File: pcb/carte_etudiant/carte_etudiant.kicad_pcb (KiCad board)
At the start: 2 copper layers, 76 x 83 mm, 5 parts, among them J1 Conn_02x15_Odd_Even, J2 Conn_01x14, J3 Conn_01x14, U1 NUCLEO64-F103RB

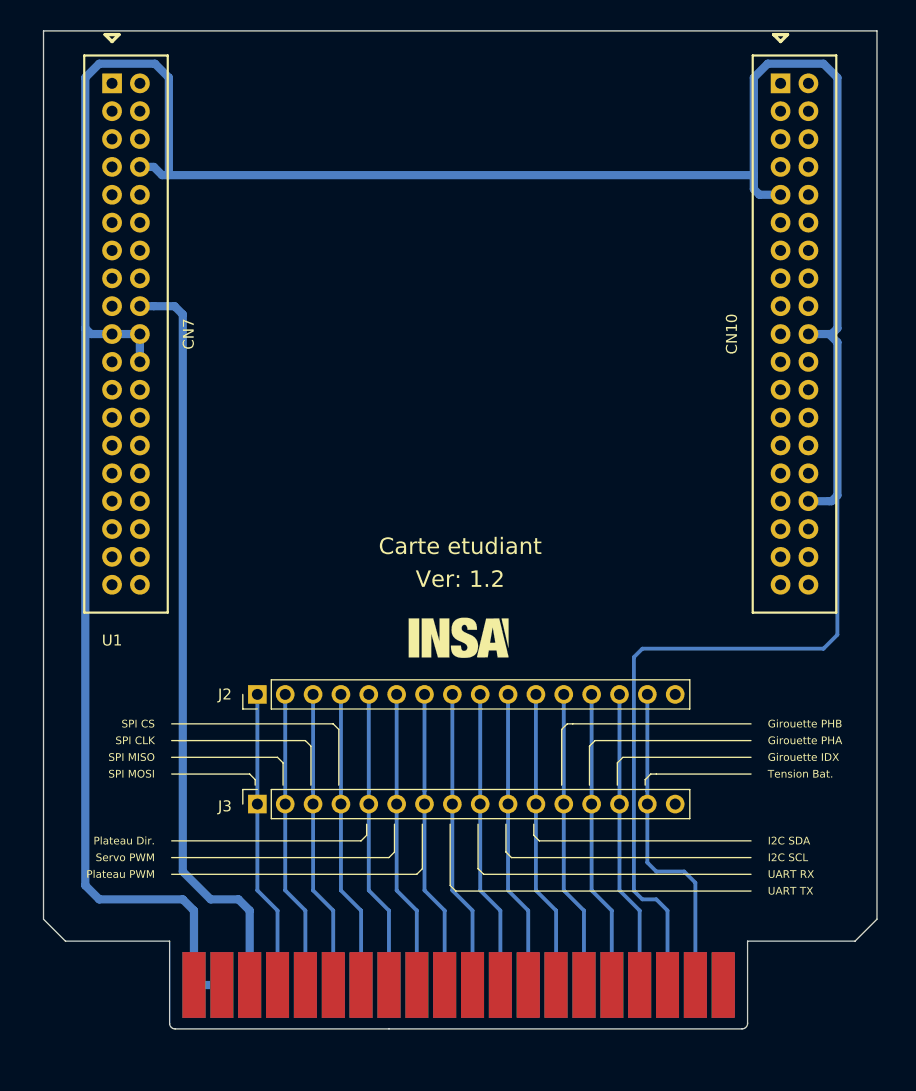
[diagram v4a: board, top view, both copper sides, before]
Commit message: Modification de la taille de la serigraphie et de son oreintation pour les cartes etudiant
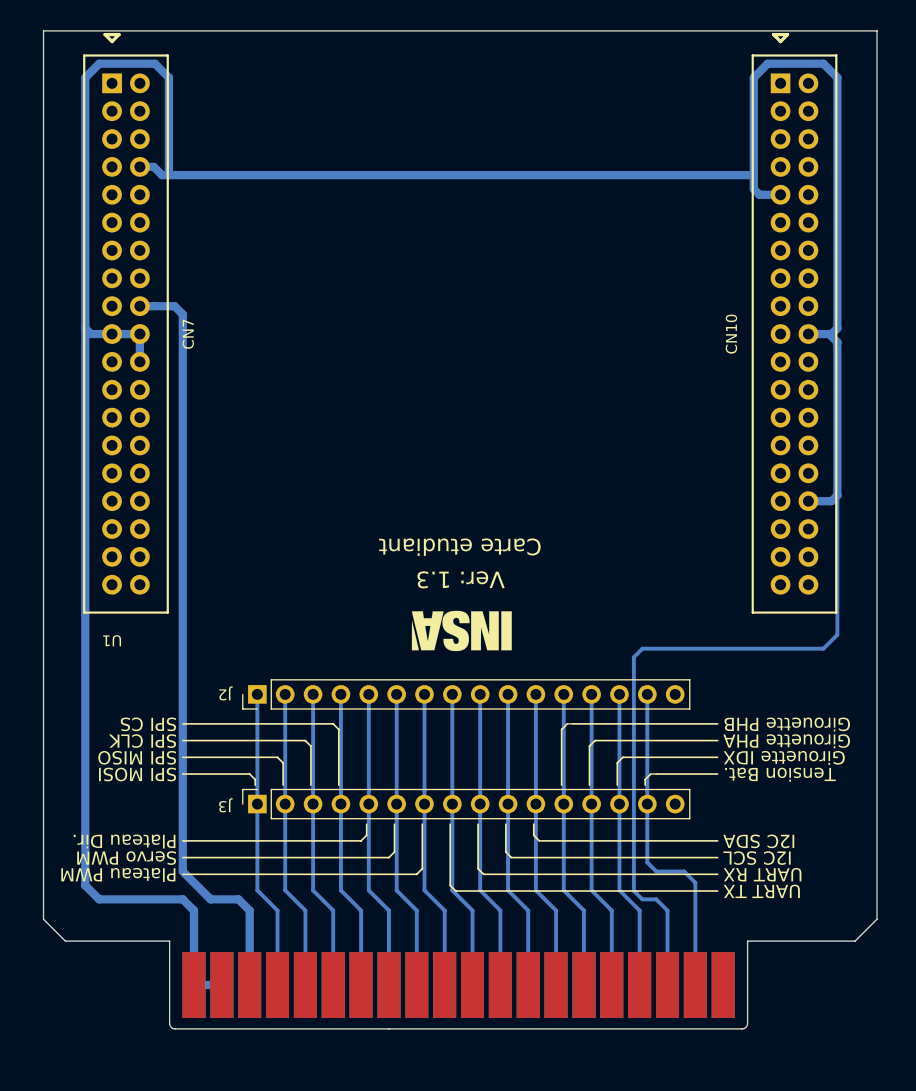
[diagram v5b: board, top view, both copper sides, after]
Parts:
- moved G*** 0.95 mm to (127.0, 117.6), turned to 180 degrees
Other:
- board text added: "Ver: 1.3"
- board text removed: "Ver: 1.2"

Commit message: rajout de plot de masse + changement taille serigraphie sur carte-etudiant
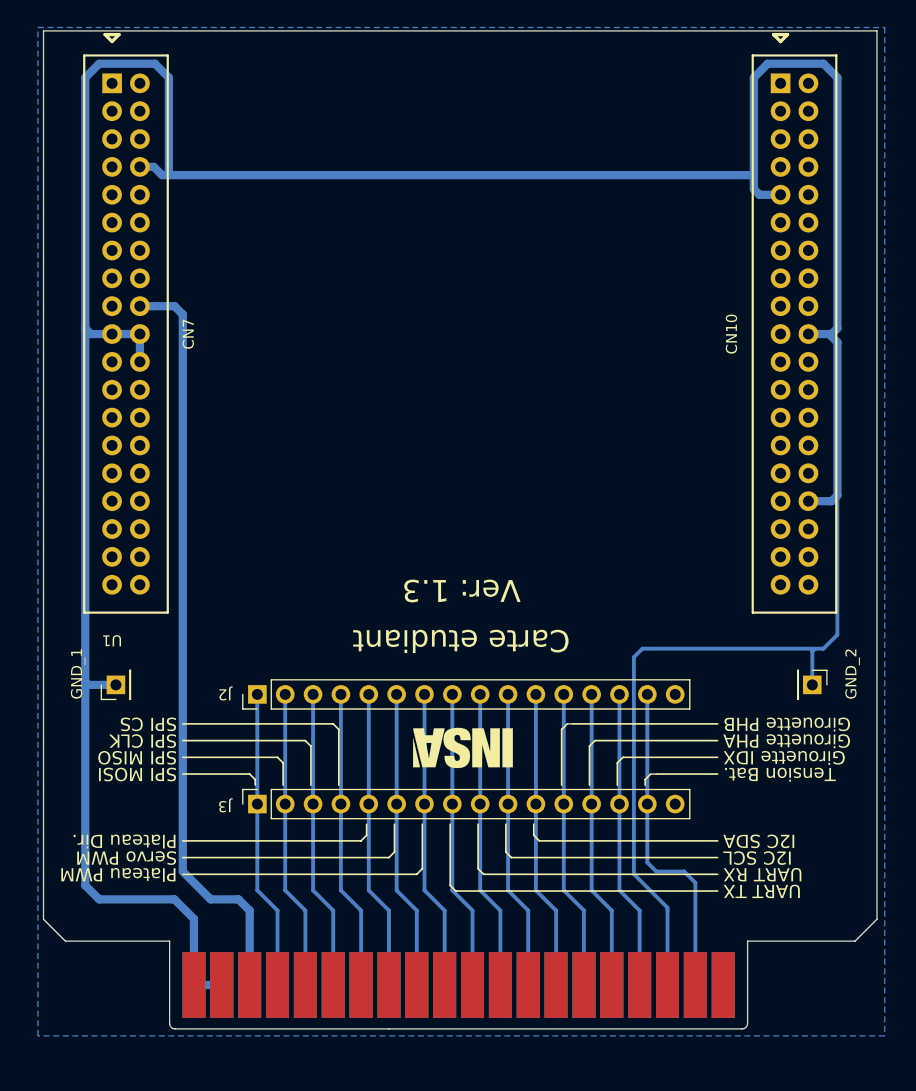
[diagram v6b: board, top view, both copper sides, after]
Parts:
- removed G***: LOGO, Insa:insa-image
- added G1: LOGO, Insa:insa-image, F.Cu at (127.1, 128.2)
- added GND_1: GND Ref, Connector_PinHeader_2.54mm:PinHeader_1x01_P2.54mm_Vertical, F.Cu at (95.6, 122.6)
- added GND_2: GND Ref, Connector_PinHeader_2.54mm:PinHeader_1x01_P2.54mm_Vertical, F.Cu at (159.1, 122.6)
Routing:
- net GND: track 304.5 -> 309.7 mm
- added copper zone on B.Cu, net GND

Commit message: Version 1.4 de la carte etudiant, ajout de la ligne SPI_CS2
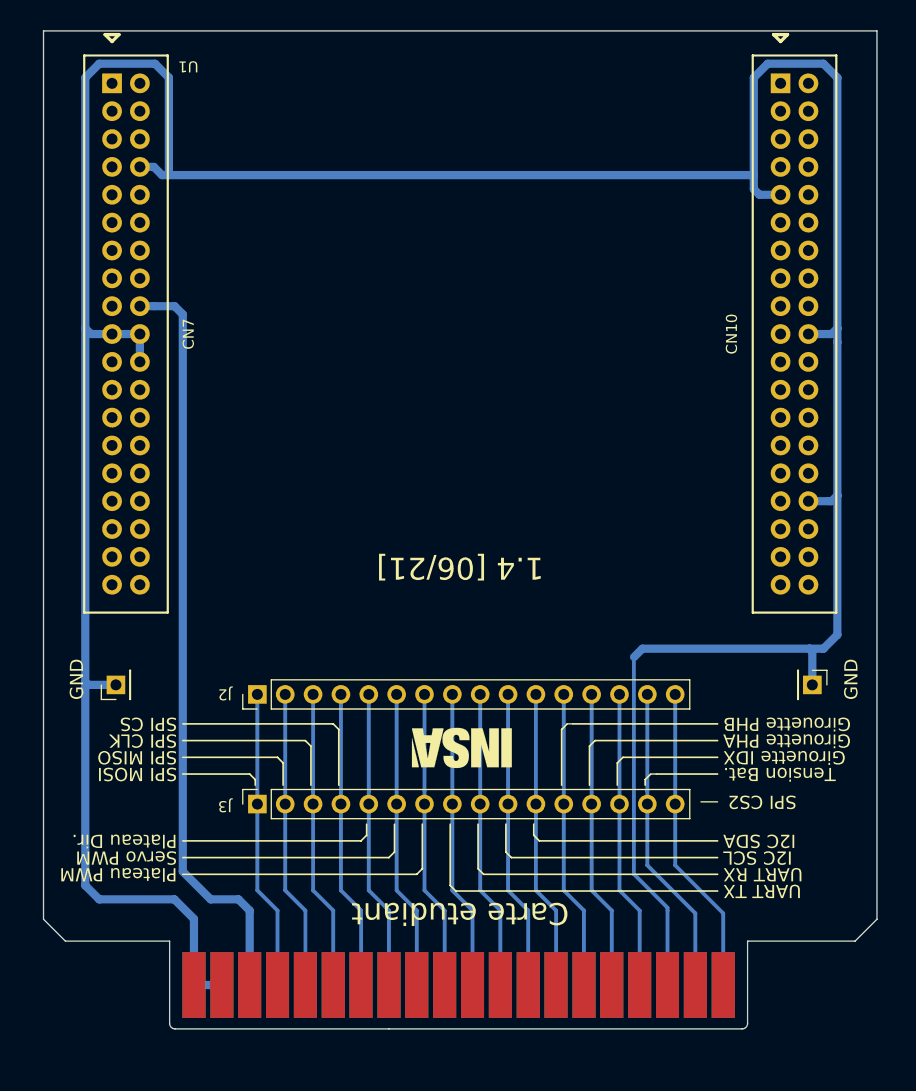
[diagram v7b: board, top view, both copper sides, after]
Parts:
- removed G1: LOGO, Insa:insa-image
- added G***: LOGO, Insa:insa-image, F.Cu at (127.0, 128.2)
- renumbered GND_2 to GND, GND_1 to GND
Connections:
- J1 pad 40: (no net) -> /SPI_CS2
- J2 pad 16: (no net) -> /SPI_CS2
- J3 pad 16: (no net) -> /SPI_CS2
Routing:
- net /SPI_CS2: track 0.00 -> 28.3 mm
- net /TENSION_BATTERIE: track 29.8 -> 28.3 mm
- removed copper zone on B.Cu, net GND
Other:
- board text added: "1.4 [06/21]"
- board text added: "SPI CS2"
- board text removed: "Ver: 1.3"

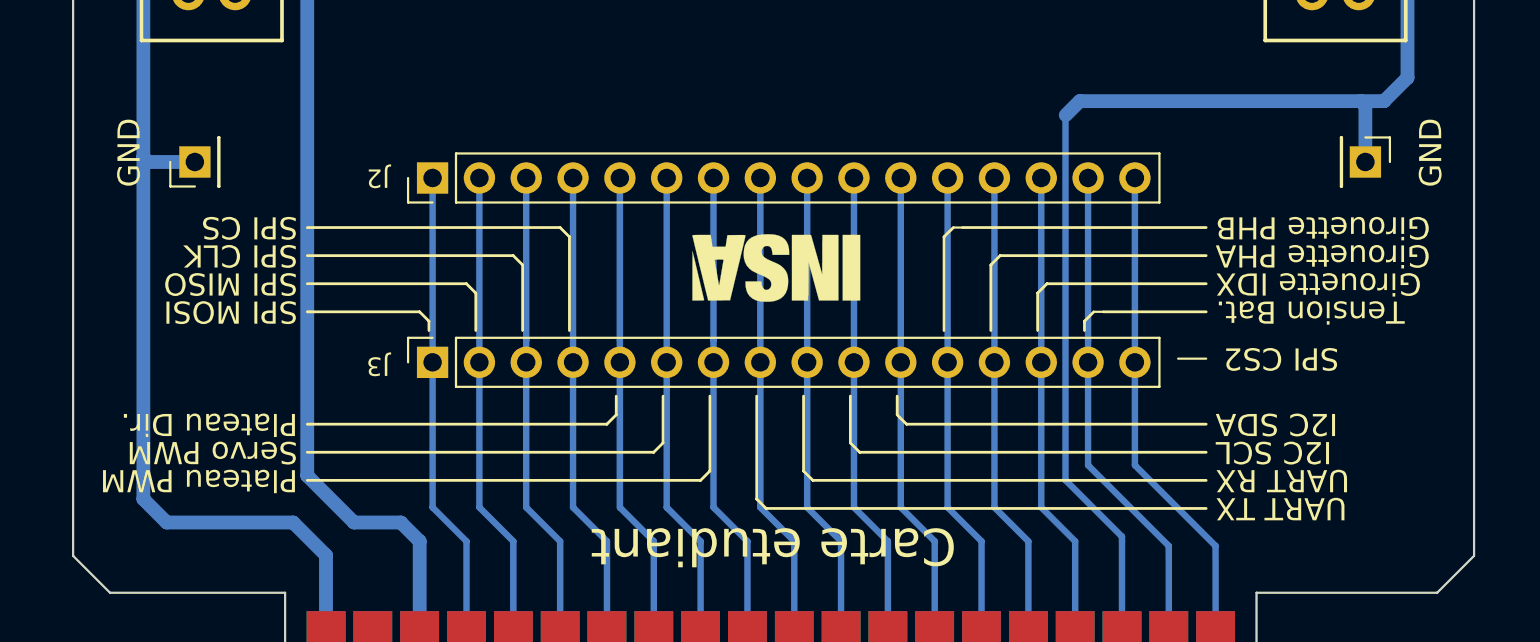
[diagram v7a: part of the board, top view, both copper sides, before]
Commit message: Envoi de la rotation toutes les 100 ms + ajout ligne spi_cs2
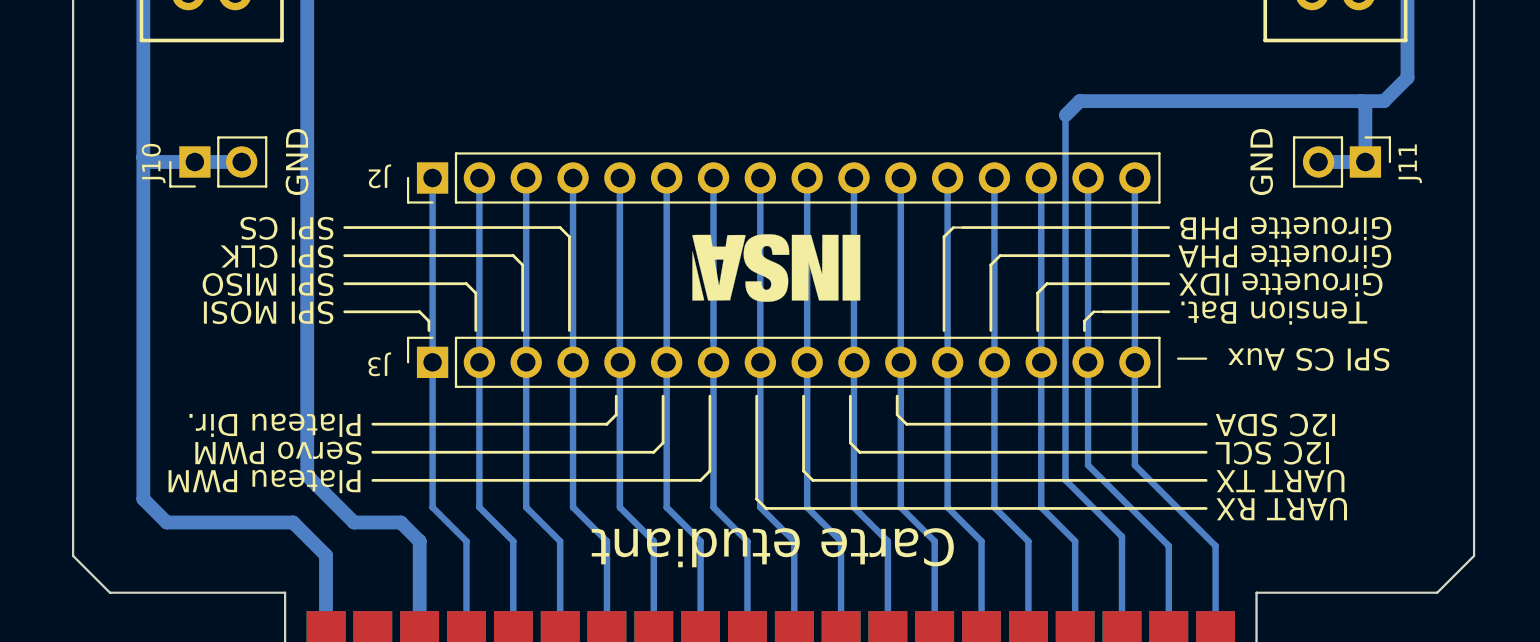
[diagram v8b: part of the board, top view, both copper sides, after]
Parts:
- removed G***: LOGO, Insa:insa-image
- removed GND (x2): GND Ref, Connector_PinHeader_2.54mm:PinHeader_1x01_P2.54mm_Vertical
- added J10: Conn_01x02, Connector_PinHeader_2.54mm:PinHeader_1x02_P2.54mm_Vertical, F.Cu at (95.6, 122.6)
- added J11: Conn_01x02, Connector_PinHeader_2.54mm:PinHeader_1x02_P2.54mm_Vertical, F.Cu at (159.1, 122.6)
- added LOGO1: Logo_Open_Hardware_Small, Insa:insa-image, F.Cu at (127.0, 128.2)
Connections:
- net /XBEE_UART_RX renamed /UART_TX
- net /XBEE_UART_TX renamed /UART_RX
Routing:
- net GND: track 309.8 -> 314.9 mm
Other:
- board text added: "GND"
- board text added: "SPI CS Aux"
- board text removed: "SPI CS2"
